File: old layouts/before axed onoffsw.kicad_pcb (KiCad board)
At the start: 4 copper layers, 65 x 56 mm, 189 parts, among them J101 Conn_01x01, J102 Conn_01x01, J1101 USB_C_Receptacle, J401 +Vbat, J402 Gnd, J403 A, J404 B, J405 C, J406 Conn_01x03, K101 SERVO, P101 CANBUS, P102 CTRL_SIGNALS, P103 Serial1/tim4, P104 I2C, P106 HALL/Encoder, P801 SWD_DEBUG, P901 I2C, Q401 Q_PNP_BCE, Q501 TPH2R608NH,L1Q, Q502 TPH2R608NH,L1Q, Q503 TPH2R608NH,L1Q, Q504 TPH2R608NH,L1Q, Q601 TPH2R608NH,L1Q, Q602 TPH2R608NH,L1Q, Q603 TPH2R608NH,L1Q, Q604 TPH2R608NH,L1Q, Q701 TPH2R608NH,L1Q, Q702 TPH2R608NH,L1Q, Q703 TPH2R608NH,L1Q, Q704 TPH2R608NH,L1Q, SW801 SW_Push, U201 MAX3051, U301 TPS561201, U401 DRV8353RSRGZT, U801 STM32F40X_LQFP64, X801 8MHz 10ppm, X802 8MHz 10ppm

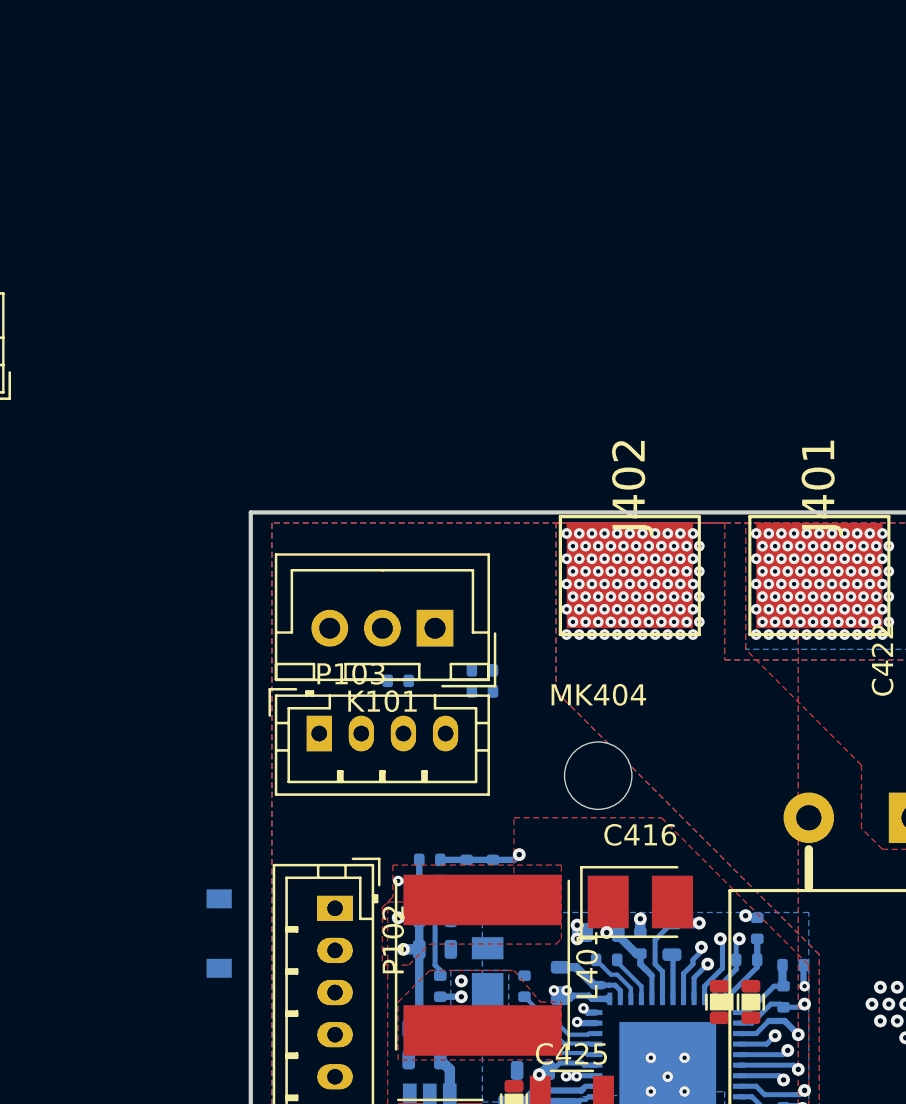
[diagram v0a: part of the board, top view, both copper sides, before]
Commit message: connector layout basically finalised. drv gate layout finished mcu layout starting
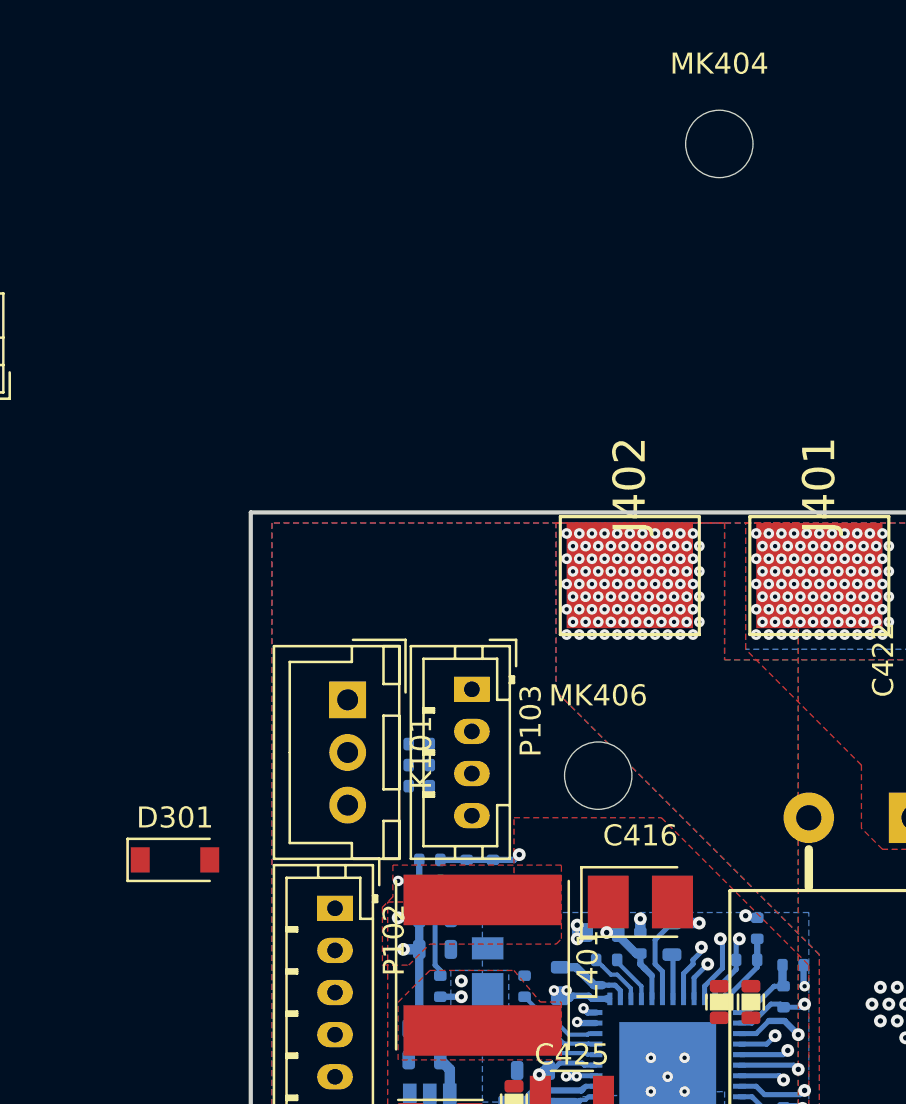
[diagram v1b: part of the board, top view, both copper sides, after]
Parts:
- added MK406: Mounting_Hole, Mounting_Holes:MountingHole_3.2mm_M3_DIN965, F.Cu at (121.0, 116.0)
- D301: moved to F.Cu
- moved MK404 30.5 mm to (126.8, 86.0)
- moved P103 7.55 mm to (115.0, 111.9), turned to 270 degrees
- moved K101 5.36 mm to (109.1, 112.4), turned to 270 degrees
- moved R101 5.10 mm to (112.5, 116.5)
- moved C101 4.61 mm to (112.5, 115.5)
- moved R102 4.61 mm to (112.5, 114.5)
- moved D301 4.08 mm to (100.9, 120.0), turned to 0 degrees
